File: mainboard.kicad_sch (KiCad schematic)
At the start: 22 parts, among them J1 HX711, J10 MainPump, J11 WaterLevelSensor, J12 AuxPump, J13 OneWireTemp, J14 OneWireTemp, J15 FlowSensor, J16 USB_C_Receptacle_USB2.0_16P, J2 Servo, J20 DC 12V IN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

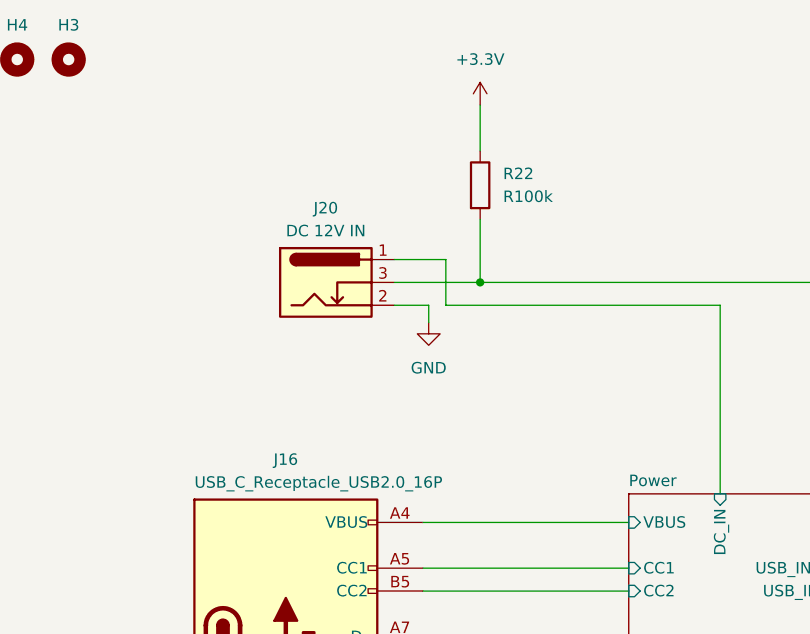
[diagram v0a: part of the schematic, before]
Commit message: Reannotate geographically by layout
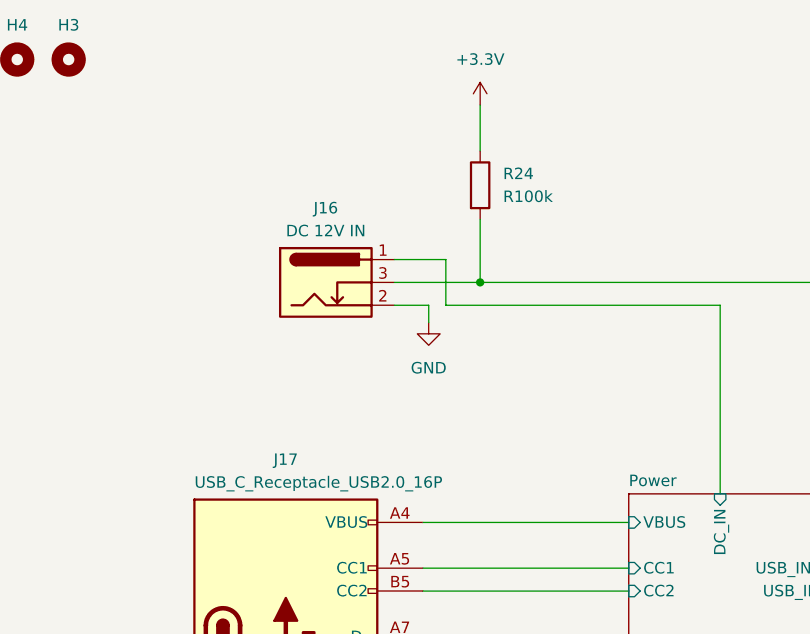
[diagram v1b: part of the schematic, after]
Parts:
- renumbered J20 to J16, J16 to J17, R22 to R24
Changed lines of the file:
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@@
   (symbol (lib_id "Connector:USB_C_Receptacle_USB2.0_16P") (at 66.675 92.075 0) (unit 1)
     (in_bom yes) (on_board yes) (dnp no)
-    (property "Reference" "J16" (at 66.675 69.85 0)
+    (property "Reference" "J17" (at 66.675 69.85 0)
       (effects (font (size 1.27 1.27)))
     )
@@
       (project "mainboard"
         (path "/613f8c39-c37c-4981-8911-5138d36a7959"
-          (reference "J16") (unit 1)
+          (reference "J17") (unit 1)
         )
       )
@@
   (symbol (lib_id "Device:R") (at 88.265 39.37 0) (unit 1)
     (in_bom yes) (on_board yes) (dnp no) (fields_autoplaced)
-    (property "Reference" "R22" (at 90.805 38.1 0)
+    (property "Reference" "R24" (at 90.805 38.1 0)
       (effects (font (size 1.27 1.27)) (justify left))
     )
@@
       (project "mainboard"
         (path "/613f8c39-c37c-4981-8911-5138d36a7959"
-          (reference "R22") (unit 1)
+          (reference "R24") (unit 1)
         )
       )
@@
   (symbol (lib_id "Connector:Barrel_Jack_Switch") (at 71.12 50.165 0) (unit 1)
     (in_bom yes) (on_board yes) (dnp no) (fields_autoplaced)
-    (property "Reference" "J20" (at 71.12 41.91 0)
+    (property "Reference" "J16" (at 71.12 41.91 0)
       (effects (font (size 1.27 1.27)))
     )
@@
       (project "mainboard"
         (path "/613f8c39-c37c-4981-8911-5138d36a7959"
-          (reference "J20") (unit 1)
-        )
-      )
+          (reference "J16") (unit 1)
+        )
+      )

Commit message: Final checks and cleanup
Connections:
- net +12V: no longer J11.1 (Pin_1)
- net +3.3V: now also J11.1 (Pin_1)
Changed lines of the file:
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@@
     (title "openautolab - Mainboard")
     (date "2024-04-03")
-    (rev "1.0")
+    (rev "2.0")
   )
   (junction (at 66.675 117.475) (diameter 0) (color 0 0 0 0)
@@
     )
   )
+  (symbol (lib_id "power:+3.3V") (at 273.05 118.11 0) (mirror y) (unit 1)
+    (in_bom yes) (on_board yes) (dnp no) (fields_autoplaced)
+    (property "Reference" "#PWR011" (at 273.05 121.92 0)
+      (effects (font (size 1.27 1.27)) hide)
+    )
+    (property "Value" "+3.3V" (at 273.05 113.03 0)
+      (effects (font (size 1.27 1.27)))
+    )
+    (property "Footprint" "" (at 273.05 118.11 0)
+      (effects (font (size 1.27 1.27)) hide)
+    )
+    (property "Datasheet" "" (at 273.05 118.11 0)
+      (effects (font (size 1.27 1.27)) hide)
+    )
+    (pin "1")
+    (instances
+      (project "mainboard"
+        (path "/613f8c39-c37c-4981-8911-5138d36a7959"
+          (reference "#PWR011") (unit 1)
+        )
+      )
+    )
+  )
   (symbol (lib_id "Connector_Generic:Conn_01x02") (at 364.49 100.33 0) (unit 1)
     (in_bom yes) (on_board yes) (dnp no) (fields_autoplaced)
@@
         )
       )
-    )
-  )
-  (symbol (lib_id "power:+12V") (at 273.05 118.11 0) (unit 1)
-    (in_bom yes) (on_board yes) (dnp no) (fields_autoplaced)
-    (property "Reference" "#PWR043" (at 273.05 121.92 0)
-      (effects (font (size 1.27 1.27)) hide)
-    )
-    (property "Value" "+12V" (at 273.05 113.665 0)
-      (effects (font (size 1.27 1.27)))
-    )
-    (property "Footprint" "" (at 273.05 118.11 0)
-      (effects (font (size 1.27 1.27)) hide)
-    )
-    (property "Datasheet" "" (at 273.05 118.11 0)
-      (effects (font (size 1.27 1.27)) hide)
-    )
-    (pin "1")
-    (instances
-      (project "mainboard"
-        (path "/613f8c39-c37c-4981-8911-5138d36a7959"
-          (reference "#PWR043") (unit 1)
-        )
-      )

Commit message: Fix revision
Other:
- title: openautolab - Mainboard -> openautolab - Alternative Mainboard
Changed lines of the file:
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@@
   (paper "A3")
   (title_block
-    (title "openautolab - Mainboard")
+    (title "openautolab - Alternative Mainboard")
     (date "2024-04-03")
-    (rev "2.0")
+    (rev "1")
   )
   (junction (at 66.675 117.475) (diameter 0) (color 0 0 0 0)
